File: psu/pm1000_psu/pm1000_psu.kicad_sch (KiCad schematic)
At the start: 35 parts, among them J1 44V A, J2 44V B, J3 Screw_Terminal_01x04, J4 48V phantom, U1 LM317_TO-220, U2 LM317_TO-220, U3 LM317_TO-220

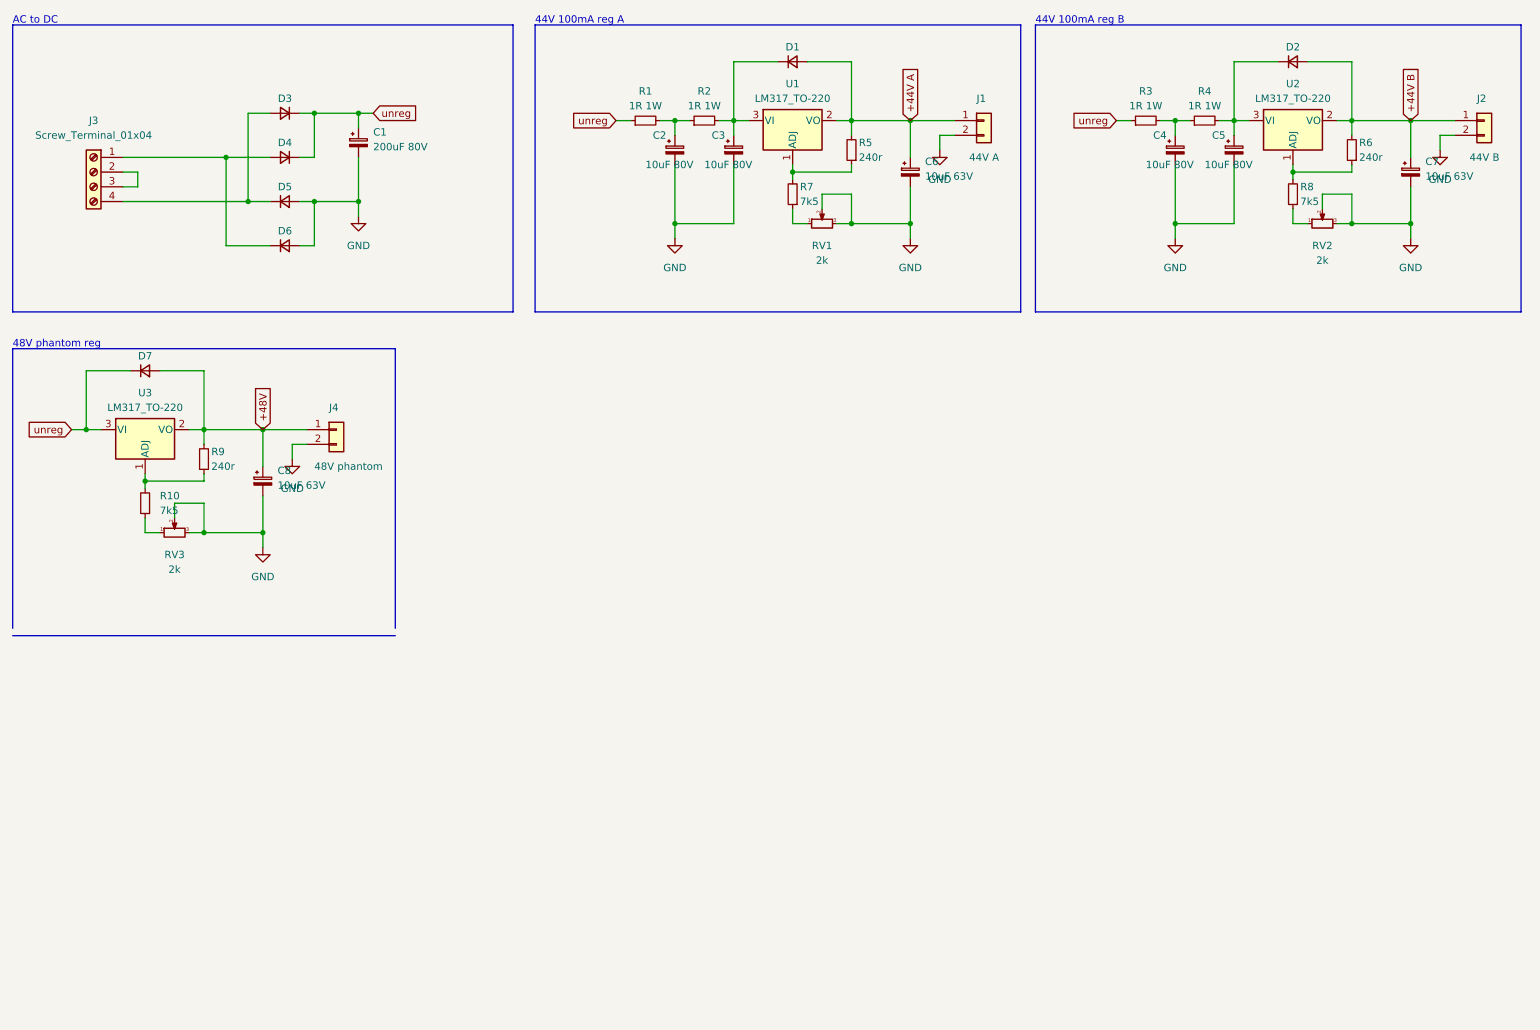
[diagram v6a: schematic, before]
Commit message: update boms with (some) mouser part numbers add 100n capacitors add power leds add frontpanel power led connector to psu board
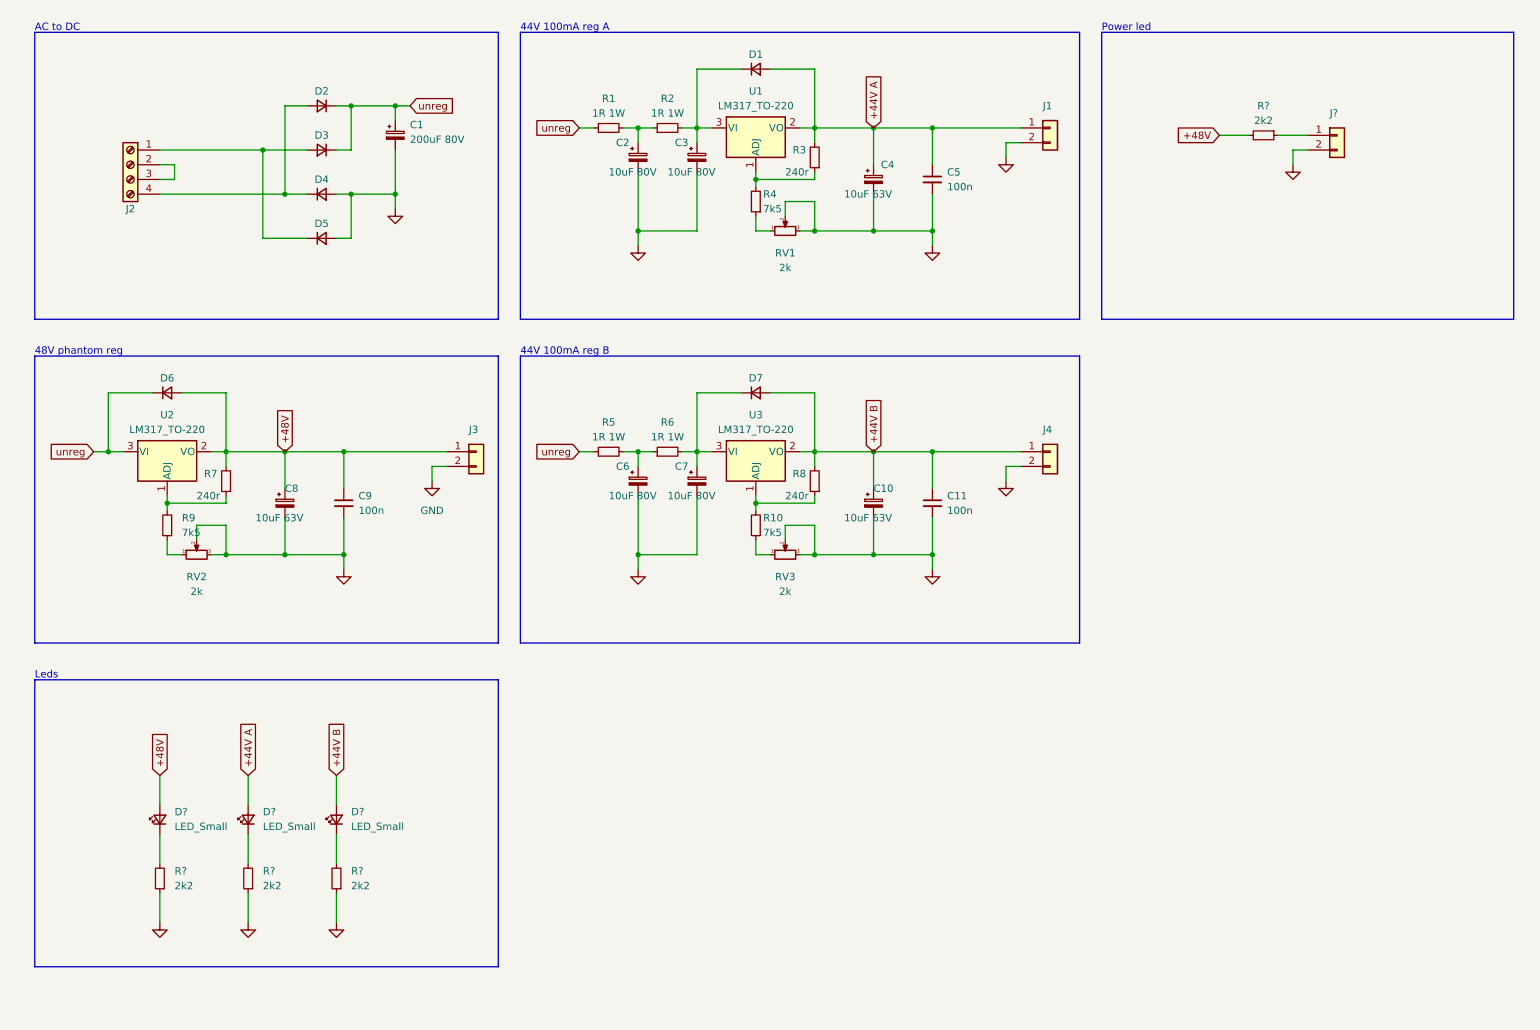
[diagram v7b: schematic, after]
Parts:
- added C11, C5, C9: 100n, Capacitor_THT:C_Disc_D5.0mm_W2.5mm_P2.50mm, symbol Device:C_Small
- added D? (x3): LED_Small, LED_THT:LED_D3.0mm, symbol Device:LED_Small
- added J?: (no value), Connector_Molex:Molex_KK-254_AE-6410-02A_1x02_P2.54mm_Vertical, symbol Connector_Generic:Conn_01x02
- added R? (x4): 2k2, Resistor_THT:R_Axial_DIN0207_L6.3mm_D2.5mm_P10.16mm_Horizontal, symbol Device:R_Small
- J1: value 44V A -> (none); Function (none) -> 44V A
- J2: renamed from J3; value Screw_Terminal_01x04 -> (none); Function (none) -> Screw_Terminal_01x04
- J3: renamed from J4; value 48V phantom -> (none); Function (none) -> 48V phantom
- J4: renamed from J2; value 44V B -> (none); Function (none) -> 44V B
- R1, R2: footprint Resistor_THT:R_Axial_DIN0207_L6.3mm_D2.5mm_P10.16mm_Horizontal -> Resistor_THT:R_Axial_DIN0414_L11.9mm_D4.5mm_P20.32mm_Horizontal; Mouser # (none) -> 603-MFR100FTE52-1R
- R10: renamed from R8; Mouser # (none) -> 603-MFR-25FRF52-7K5
- R3: renamed from R5; Mouser # (none) -> 603-MFR-25FRF52-240R
- R4: renamed from R7; Mouser # (none) -> 603-MFR-25FRF52-7K5
- R5: renamed from R3; footprint Resistor_THT:R_Axial_DIN0207_L6.3mm_D2.5mm_P10.16mm_Horizontal -> Resistor_THT:R_Axial_DIN0414_L11.9mm_D4.5mm_P20.32mm_Horizontal; Mouser # (none) -> 603-MFR100FTE52-1R
- R6: renamed from R4; footprint Resistor_THT:R_Axial_DIN0207_L6.3mm_D2.5mm_P10.16mm_Horizontal -> Resistor_THT:R_Axial_DIN0414_L11.9mm_D4.5mm_P20.32mm_Horizontal; Mouser # (none) -> 603-MFR100FTE52-1R
- R7: renamed from R9; Mouser # (none) -> 603-MFR-25FRF52-240R
- R8: renamed from R6; Mouser # (none) -> 603-MFR-25FRF52-240R
- R9: renamed from R10; Mouser # (none) -> 603-MFR-25FRF52-7K5
- U1: Mouser # (none) -> 511-LM317BT
- U2: renamed from U3; Mouser # (none) -> 511-LM317BT
- U3: renamed from U2; Mouser # (none) -> 511-LM317BT
- renumbered C7 to C10, C6 to C4, C4 to C6, C5 to C7, D3 to D2, D4 to D3, D5 to D4, D6 to D5, D7 to D6, D2 to D7, RV3 to RV2, RV2 to RV3
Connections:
- net +44V A: now also C5.1, D?.2 (A)
- net +44V B: now also C11.1, D?.2 (A)
- net +48V: now also C9.1, D?.2 (A), R?.2
- net GND: now also C11.2, C5.2, C9.2, J?.2 (Pin_2), R?.1, R?.1, R?.1
- new net: D?.1 (K), R?.2 (x3)
- new net: J?.1 (Pin_1), R?.1
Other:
- note added: "Leds"
- note added: "Power led"
- moved on the sheet: C1, C10, C2, C3, C4, C6, C7, C8, D1, D2, D3, D4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

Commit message: add power pins for cpu
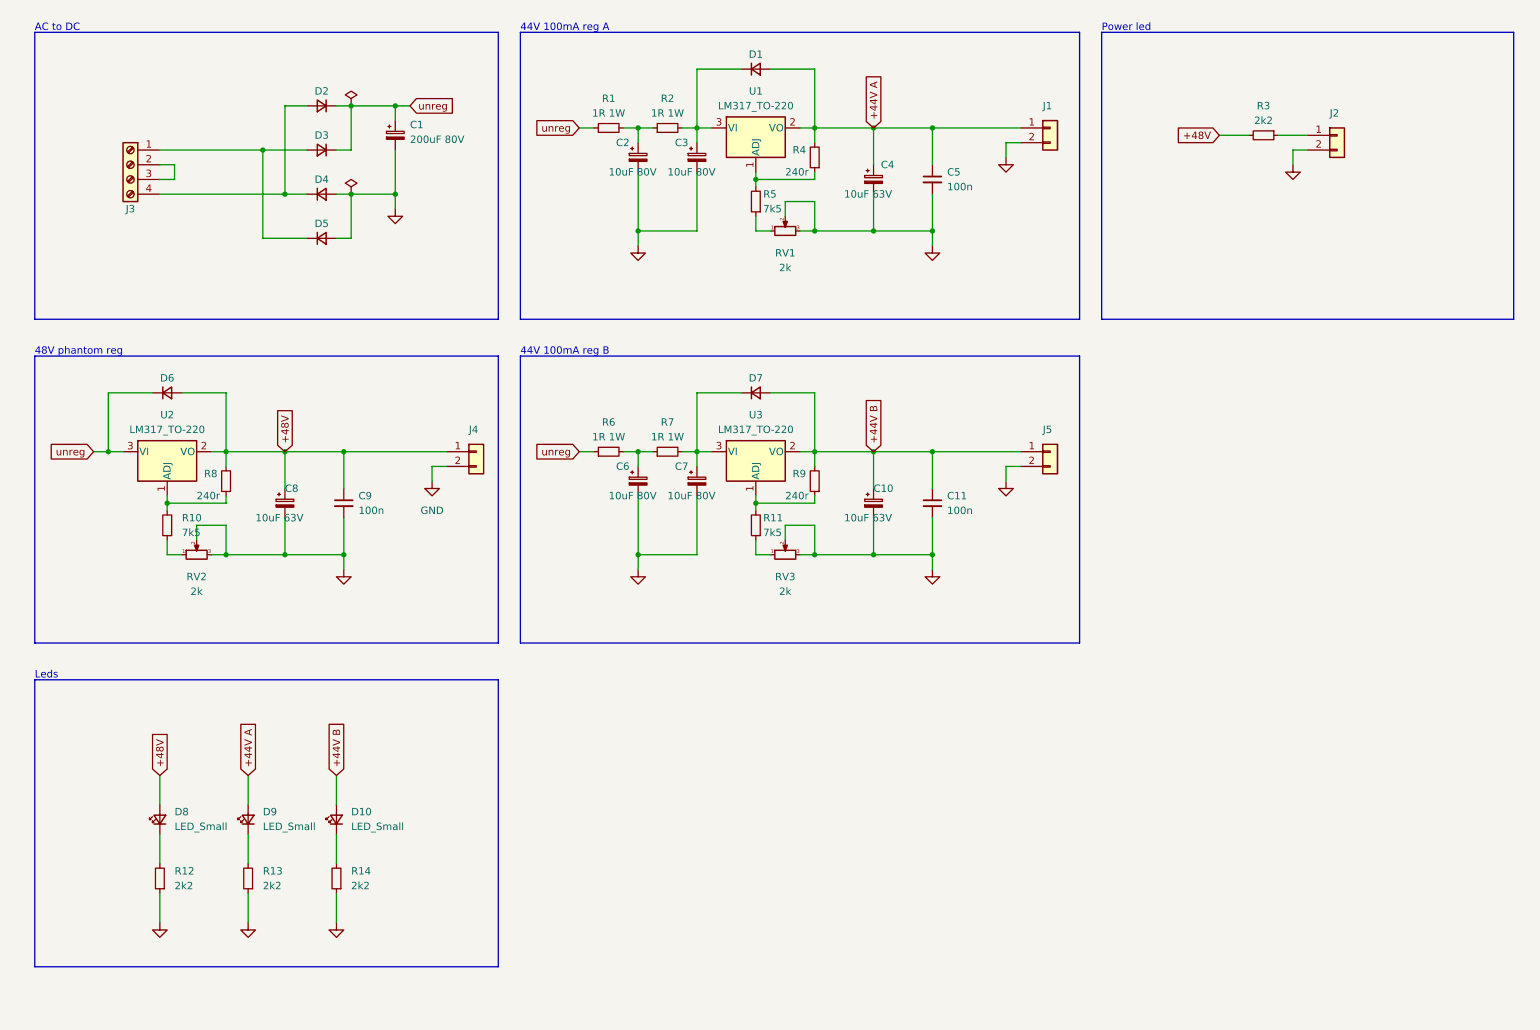
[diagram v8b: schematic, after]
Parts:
- gave numbers to parts that had none: 8
- renumbered J2 to J3, J3 to J4, J4 to J5, R9 to R10, R10 to R11, R3 to R4, R4 to R5, R5 to R6, R6 to R7, R7 to R8, R8 to R9
